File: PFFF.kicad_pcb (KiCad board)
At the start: 2 copper layers, 25 x 22.9 mm, 14 parts, among them J1 Conn_01x02, J2 Conn_01x02, J3 Conn_01x03, J4 Conn_01x03, U1 TPS61099YFFT

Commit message: fake change
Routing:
- net GND: vias 35 -> 36
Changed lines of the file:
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@@
+	)
+	(via
+		(at 136.9 87.6)
+		(size 0.8)
+		(drill 0.4)
+		(layers "F.Cu" "B.Cu")
+		(free yes)
+		(net 2)
 	)
 	(via

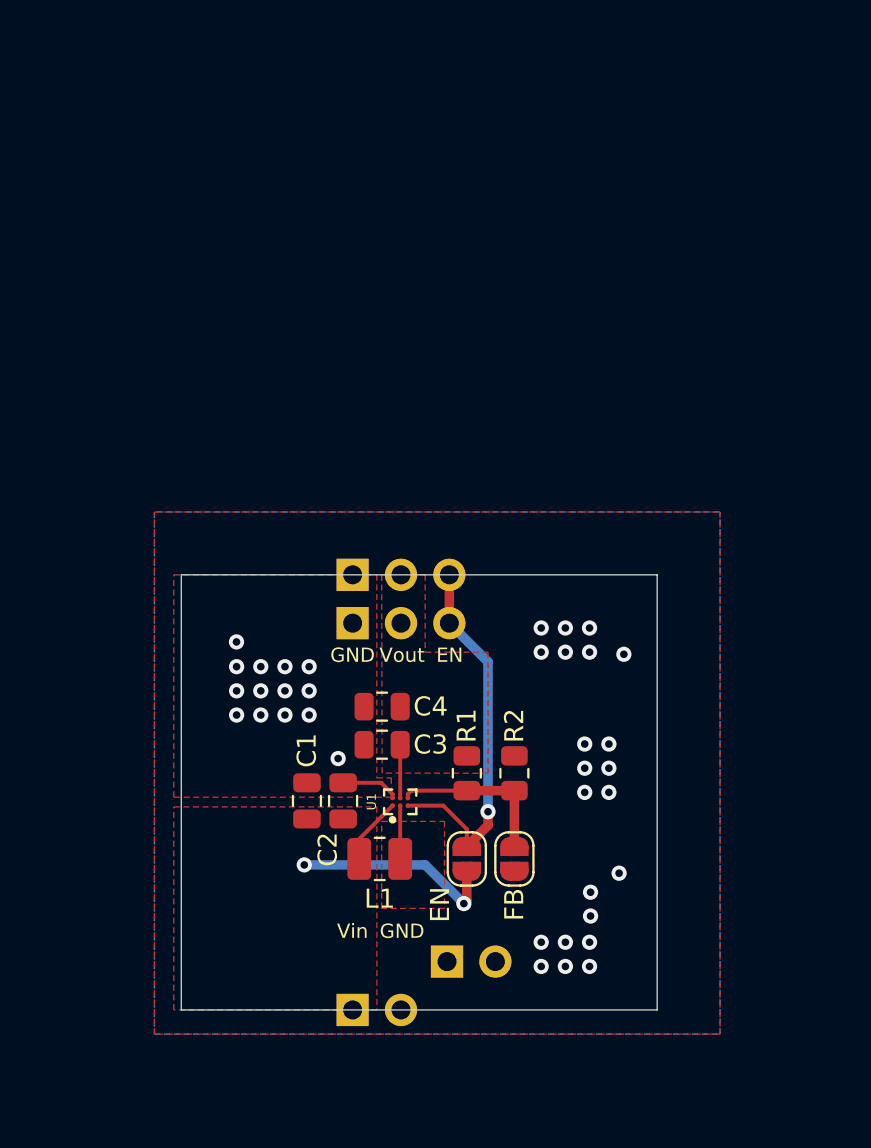
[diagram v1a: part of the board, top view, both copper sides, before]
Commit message: add all USB Type-C
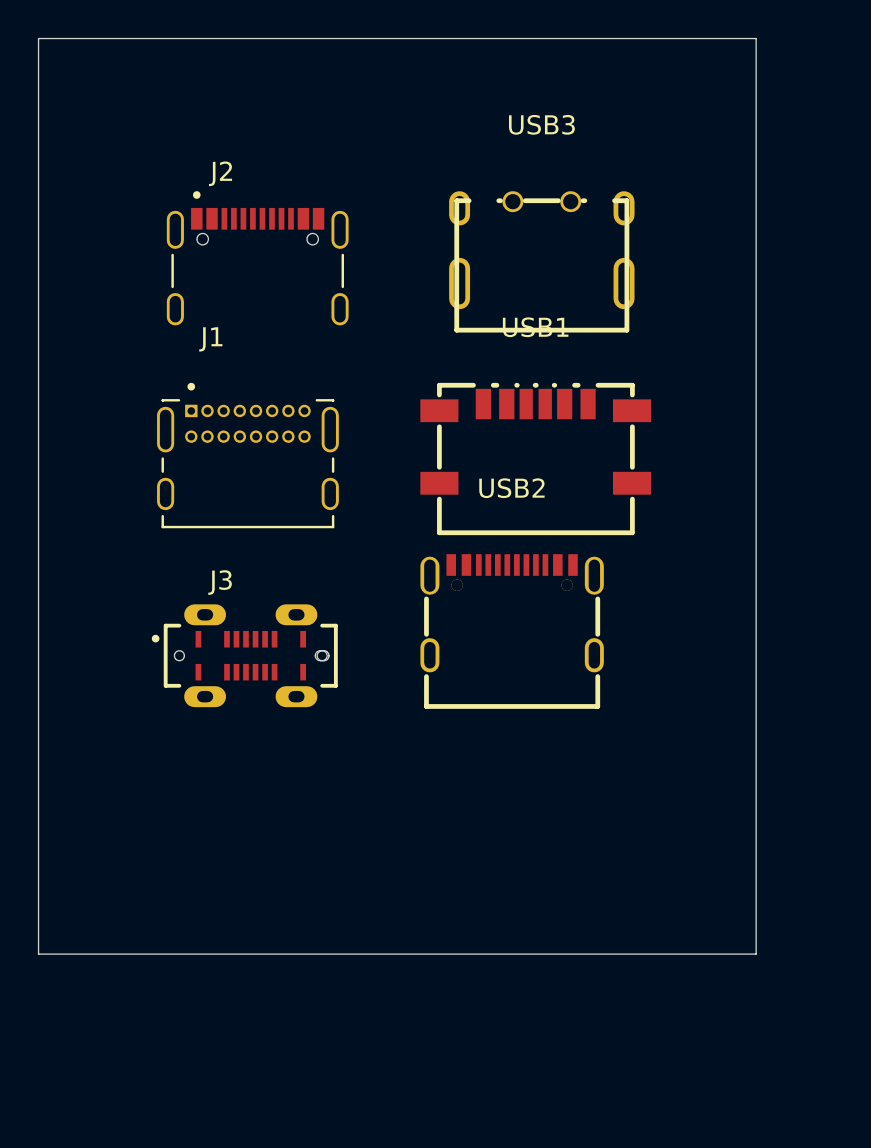
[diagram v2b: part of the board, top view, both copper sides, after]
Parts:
- removed C1, C2, C3, C4: C_Small, Capacitor_SMD:C_0805_2012Metric
- removed J4: Conn_01x03, Connector_PinHeader_2.54mm:PinHeader_1x03_P2.54mm_Vertical
- removed JP1, JP2: SolderJumper_2_Open, Jumper:SolderJumper-2_P1.3mm_Open_RoundedPad1.0x1.5mm
- removed L1: L_Small, Inductor_SMD:L_1008_2520Metric
- removed R1, R2: R_Small, Resistor_SMD:R_0805_2012Metric
- removed U1: TPS61099YFFT, Converter_DCDC_custom:BGA6N40P3X2_122X88X62N
- added USB1: TYPE-C-31-M-29, Snapeda:easyeda2kicad_USB-C-SMD_TYPE-C-31-M-29, F.Cu at (152.6, 77.2)
- added USB2: TYPE-C-31-M-31, Snapeda:easyeda2kicad_USB-C-SMD_TYPE-C-31-M-31, F.Cu at (151.4, 85.9)
- added USB3: TYPE-C-31-M-33, Snapeda:easyeda2kicad_USB-C-TH_TYPE-C-31-M-33, F.Cu at (152.9, 66.6)
- J1: value Conn_01x02 -> UJ20-C-H-G-SMT-TR; footprint Connector_PinHeader_2.54mm:PinHeader_1x02_P2.54mm_Vertical -> Snapeda:UJ20-C-H-G-SMT-TR_CUI_UJ20-C-H-G-SMT-TR
- J2: value Conn_01x02 -> TYPE-C-31-M-12; footprint Connector_PinHeader_2.54mm:PinHeader_1x02_P2.54mm_Vertical -> Snapeda:TYPE-C-31-M-12_HRO_TYPE-C-31-M-12
- J3: value Conn_01x03 -> USB4120-03-C_REVA; footprint Connector_PinHeader_2.54mm:PinHeader_1x03_P2.54mm_Vertical -> Snapeda:USB4120-03-C_REVA_GCT_USB4120-03-C_REVA
- moved J2 37.2 mm to (138.0, 70.1), turned to 0 degrees
- moved J1 27.0 mm to (137.5, 79.5), turned to 0 degrees
- moved J3 5.62 mm to (137.7, 88.3), turned to 0 degrees
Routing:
- net En: track 19.9 -> 0.00 mm, vias 1 -> 0
- net Vin: track 14.5 -> 0.00 mm, vias 2 -> 0
- net FB: track 8.82 -> 0.00 mm
- net GND: track 3.05 -> 0.00 mm, vias 36 -> 0
- net Vout: track 2.80 -> 0.00 mm
- net SW: track 2.80 -> 0.00 mm
- removed copper zone on B.Cu, net GND
- removed copper zone on F.Cu, net GND
- removed copper zone on F.Cu, net SW
- removed copper zone on F.Cu, net Vin
- removed copper zone on F.Cu, net Vout
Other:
- board size 25 x 22.9 mm -> 37.7 x 48.1 mm
- board text removed: "EN"
- board text removed: "GND"
- board text removed: "Vin"
- board text removed: "Vout"
